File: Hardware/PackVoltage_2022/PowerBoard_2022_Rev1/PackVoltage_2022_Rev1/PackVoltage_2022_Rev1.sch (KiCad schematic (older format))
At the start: 38 parts

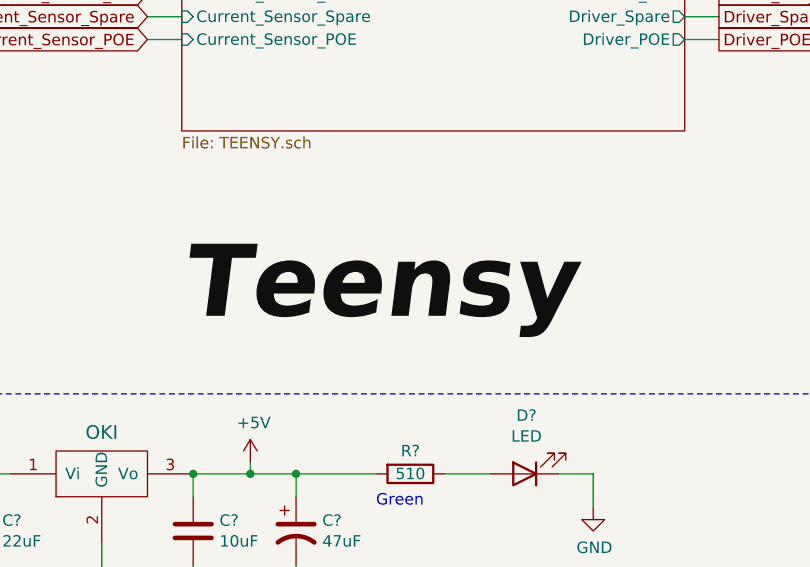
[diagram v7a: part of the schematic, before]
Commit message: Implementing the tiva into Pack
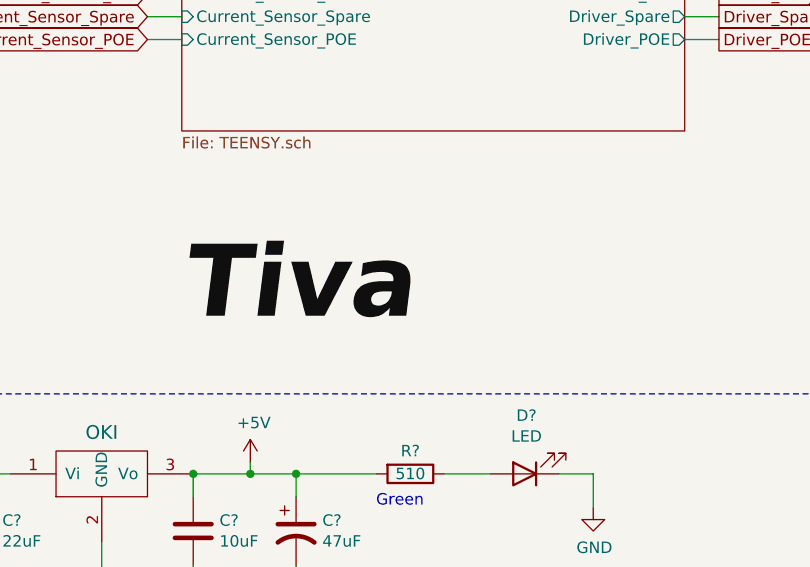
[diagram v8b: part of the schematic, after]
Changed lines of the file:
@@
 EESchema Schematic File Version 4
-LIBS:PackVoltage_2022_Rev1-cache
 EELAYER 30 0
 EELAYER END
@@
 Bucks&Mosfets
 Text Label 1900 2750 0    315  Italic 63
-Teensy
+Tiva
 Wire Wire Line
 	4100 750  4250 750
